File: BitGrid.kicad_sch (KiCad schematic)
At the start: 5 parts, among them U1 74HC164, U2 74LS151, U3 74LS75, U4 74HC164, U5 74LS151

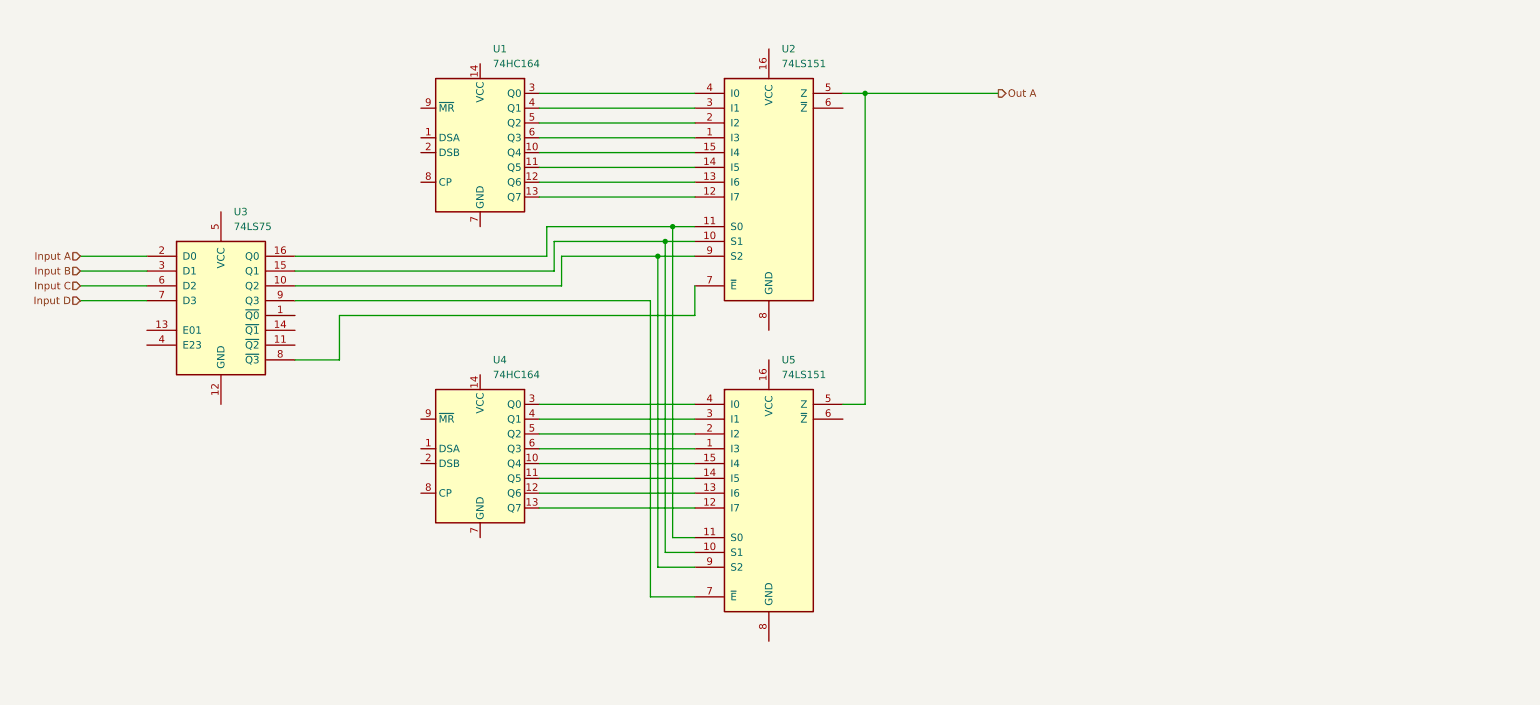
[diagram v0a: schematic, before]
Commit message: add schematic, scan chain I/O
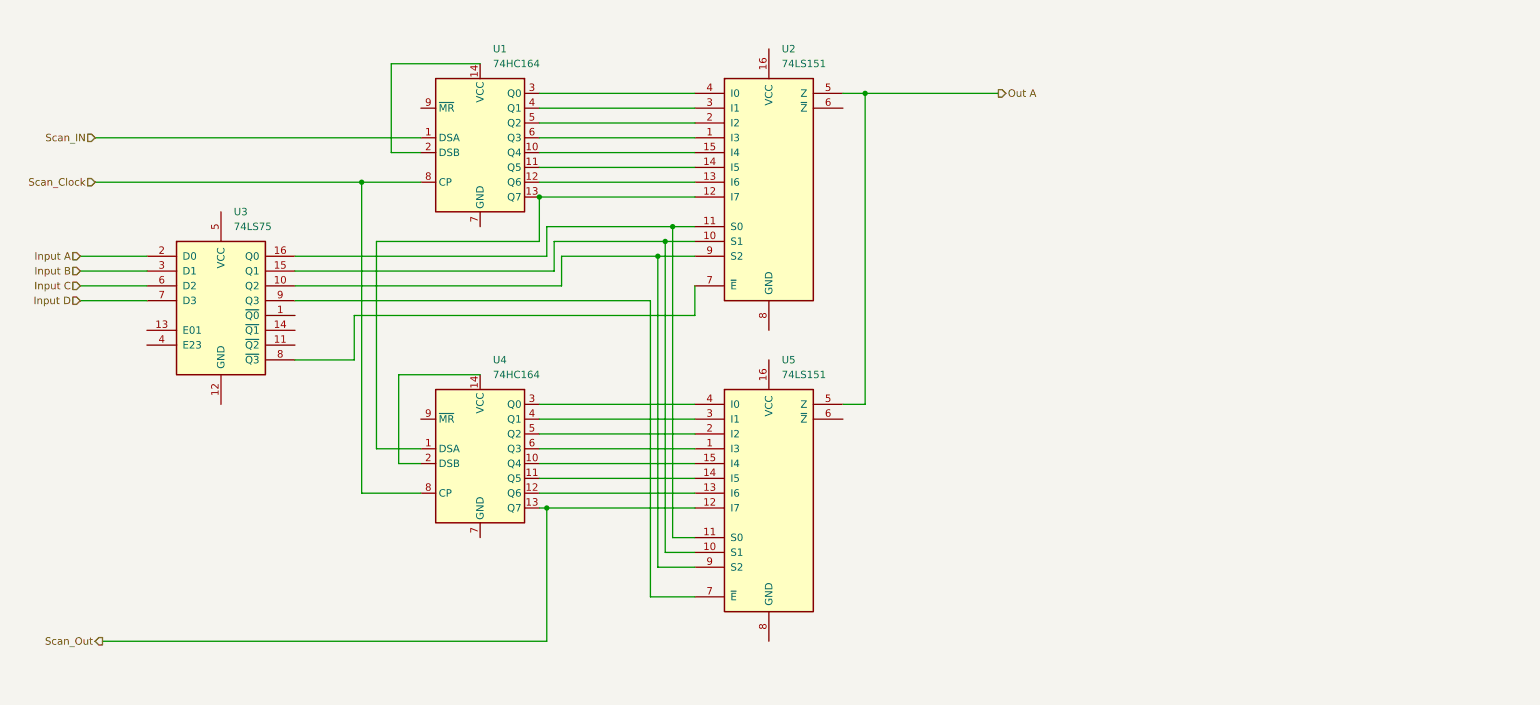
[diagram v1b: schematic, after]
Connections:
- net Scan_IN: now reaches U1.1 (DSA)
- net at U1.13 (Q7), U2.12 (I7): now also U4.1 (DSA)
- net at U1.14 (VCC): now also U1.2 (DSB)
- net Scan_Clock: now reaches U1.8 (CP)
- net Scan_Clock: now also U4.8 (CP)
- net Scan_Out: now reaches U4.13 (Q7), U5.12 (I7)
- net at U4.14 (VCC): now also U4.2 (DSB)

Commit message: add output select, to allow memory mode
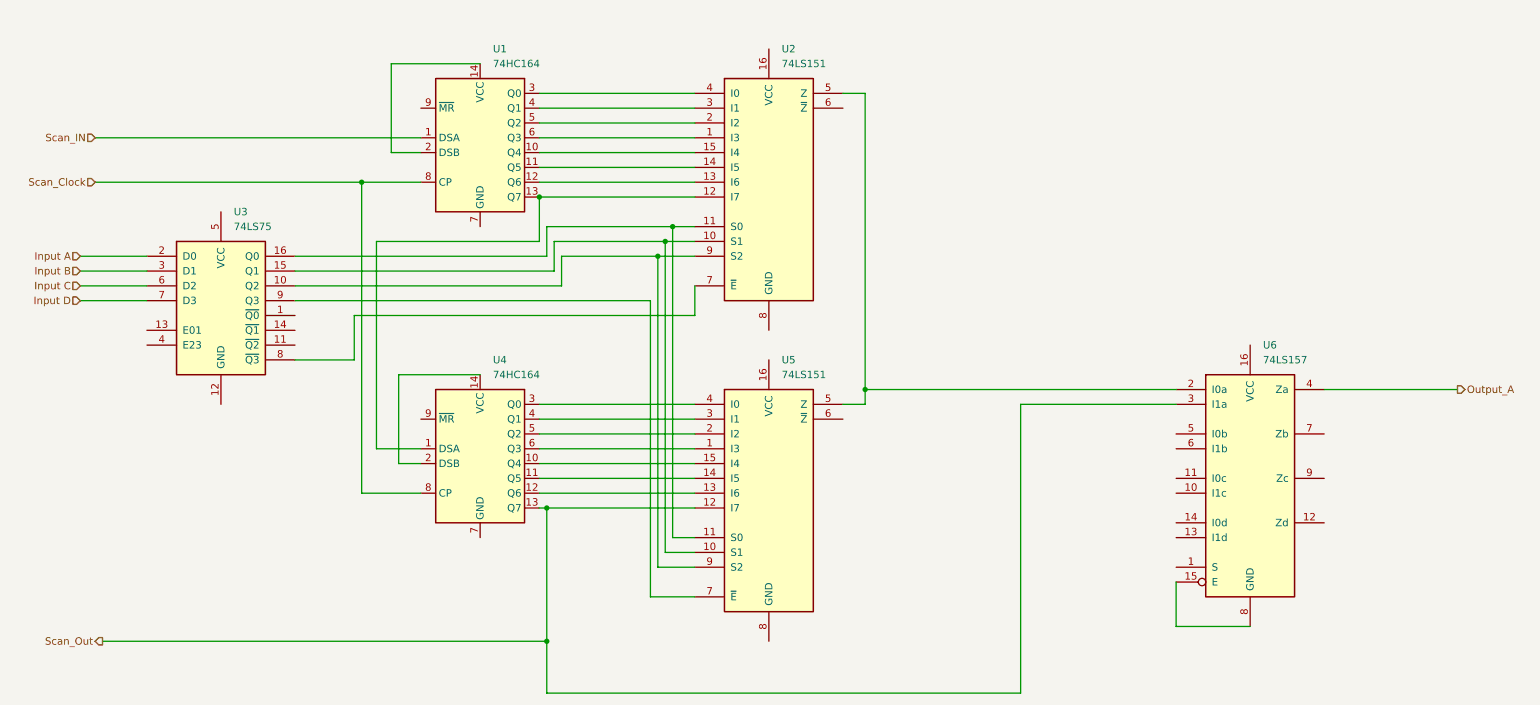
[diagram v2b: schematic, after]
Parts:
- added U6: 74LS157, symbol 74xx:74LS157
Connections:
- net Scan_Out: now also U6.3 (I1a)
- net Out A: no longer names the net of U2.5 (Z), U5.5 (Z)
- net Out A: now also U6.2 (I0a)
- new net: U6.15 (E), U6.8 (GND)
- new net Output_A: U6.4 (Za)
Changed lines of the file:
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@@
+	)
+	(junction
+		(at 102.87 119.38)
+		(diameter 0)
+		(color 0 0 0 0)
 	)
 	(junction
@@
 	)
 	(junction
-		(at 157.48 25.4)
+		(at 157.48 76.2)
 		(diameter 0)
 		(color 0 0 0 0)
@@
 	(wire
 		(pts
+			(xy 210.82 116.84) (xy 223.52 116.84)
+		)
+		(stroke
+			(width 0)
+			(type default)
+		)
+	)
+	(wire
+		(pts
 			(xy 22.86 58.42) (xy 34.29 58.42)
 		)
@@
 	(wire
 		(pts
+			(xy 210.82 109.22) (xy 210.82 116.84)
+		)
+		(stroke
+			(width 0)
+			(type default)
+		)
+	)
+	(wire
+		(pts
+			(xy 102.87 119.38) (xy 102.87 128.27)
+		)
+		(stroke
+			(width 0)
+			(type default)
+		)
+	)
+	(wire
+		(pts
 			(xy 22.86 53.34) (xy 34.29 53.34)
 		)
@@
 	(wire
 		(pts
-			(xy 157.48 25.4) (xy 180.34 25.4)
-		)
-		(stroke
-			(width 0)
-			(type default)
-		)
-	)
-	(wire
-		(pts
 			(xy 102.87 119.38) (xy 26.67 119.38)
 		)
@@
 	(wire
 		(pts
+			(xy 157.48 76.2) (xy 210.82 76.2)
+		)
+		(stroke
+			(width 0)
+			(type default)
+		)
+	)
+	(wire
+		(pts
 			(xy 120.65 60.96) (xy 120.65 111.76)
 		)
@@
 	(wire
 		(pts
+			(xy 184.15 78.74) (xy 210.82 78.74)
+		)
+		(stroke
+			(width 0)
+			(type default)
+		)
+	)
+	(wire
+		(pts
 			(xy 81.28 35.56) (xy 76.2 35.56)
 		)
@@
 	(wire
 		(pts
+			(xy 102.87 128.27) (xy 184.15 128.27)
+		)
+		(stroke
+			(width 0)
+			(type default)
+		)
+	)
+	(wire
+		(pts
 			(xy 101.6 35.56) (xy 128.27 35.56)
 		)
@@
 	(wire
 		(pts
-			(xy 157.48 78.74) (xy 157.48 25.4)
+			(xy 157.48 78.74) (xy 157.48 76.2)
 		)
 		(stroke
@@
 	(wire
 		(pts
+			(xy 157.48 76.2) (xy 157.48 25.4)
+		)
+		(stroke
+			(width 0)
+			(type default)
+		)
+	)
+	(wire
+		(pts
 			(xy 104.14 55.88) (xy 104.14 50.8)
 		)
@@
 	(wire
 		(pts
+			(xy 236.22 76.2) (xy 259.08 76.2)
+		)
+		(stroke
+			(width 0)
+			(type default)
+		)
+	)
+	(wire
+		(pts
 			(xy 22.86 60.96) (xy 34.29 60.96)
 		)
@@
 		(pts
 			(xy 76.2 35.56) (xy 76.2 20.32)
+		)
+		(stroke
+			(width 0)
+			(type default)
+		)
+	)
+	(wire
+		(pts
+			(xy 184.15 128.27) (xy 184.15 78.74)
 		)
 		(stroke
@@
 		)
 	)
-	(hierarchical_label "Out A"
-		(shape output)
-		(at 180.34 25.4 0)
-		(fields_autoplaced yes)
-		(effects
-			(font
-				(size 1.27 1.27)
-			)
-			(justify left)
-		)
-	)
 	(hierarchical_label "Scan_Clock"
 		(shape input)
@@
 			)
 			(justify right)
+		)
+	)
+	(hierarchical_label "Output_A"
+		(shape output)
+		(at 259.08 76.2 0)
+		(fields_autoplaced yes)
+		(effects
+			(font
+				(size 1.27 1.27)
+			)
+			(justify left)
 		)
 	)
@@
 					(unit 1)
 				)
+			)
+		)
+	)
+	(symbol
+		(lib_id "74xx:74LS157")
+		(at 223.52 91.44 0)
+		(unit 1)
+		(exclude_from_sim no)
+		(in_bom yes)
+		(on_board yes)
+		(dnp no)
+		(fields_autoplaced yes)
+		(property "Reference" "U6"
+			(at 225.7141 68.58 0)
+			(effects
+				(font
+					(size 1.27 1.27)
+				)
+				(justify left)
+			)
+		)
+		(property "Value" "74LS157"
+			(at 225.7141 71.12 0)
+			(effects
+				(font
+					(size 1.27 1.27)
+				)
+				(justify left)
+			)
+		)
+		(property "Footprint" ""
+			(at 223.52 91.44 0)
+			(effects
+				(font
+					(size 1.27 1.27)
+				)
+				(hide yes)
+			)
+		)
+		(property "Datasheet" "http://www.ti.com/lit/gpn/sn74LS157"
+			(at 223.52 91.44 0)
+			(effects
+				(font
+					(size 1.27 1.27)
+				)
+				(hide yes)
+			)
+		)
+		(property "Description" "Quad 2 to 1 line Multiplexer"
+			(at 223.52 91.44 0)
+			(effects
+				(font
+					(size 1.27 1.27)
+				)
+				(hide yes)
+			)
+		)
+		(pin "12"
+		)
+		(pin "1"
+		)
+		(pin "10"
+		)
+		(pin "13"
+		)
+		(pin "14"
+		)
+		(pin "15"
+		)
+		(pin "16"
+		)
+		(pin "2"
+		)
+		(pin "11"
+		)
+		(pin "5"
+		)
+		(pin "7"
+		)
+		(pin "3"
+		)
+		(pin "8"
+		)
+		(pin "9"
+		)
+		(pin "6"
+		)
+		(pin "4"
+		)
+		(instances
+			(project ""
+				(path "/490e8ab2-84af-4693-939c-657a58dcba0a"
+					(reference "U6")
+					(unit 1)
+				)

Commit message: connect chips to power
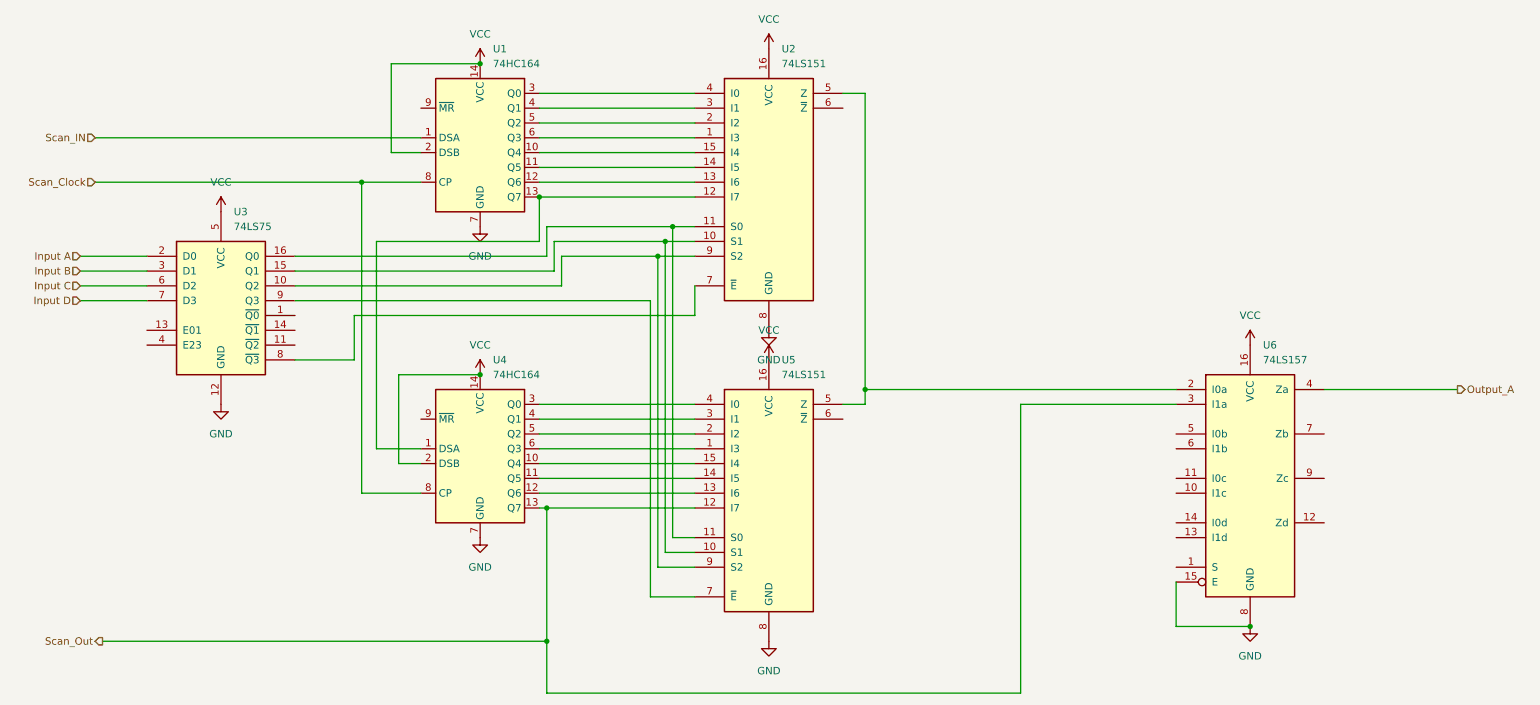
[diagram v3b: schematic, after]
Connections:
- net VCC: now reaches U1.14 (VCC), U1.2 (DSB)
- net VCC: now also U2.16 (VCC), U3.5 (VCC), U4.14 (VCC), U4.2 (DSB), U5.16 (VCC), U6.16 (VCC)
- net GND: now reaches U1.7 (GND)
- net GND: now also U2.8 (GND), U3.12 (GND), U4.7 (GND), U5.8 (GND), U6.15 (E), U6.8 (GND)
